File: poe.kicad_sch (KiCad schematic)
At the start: 59 parts, among them IC1 TPS2378DDA, J1 B2B-XH-A_LF__SN_, J6 SS-74800-144, U3 TPS2373-3RGW, U4 URB4805YMD-30WR3

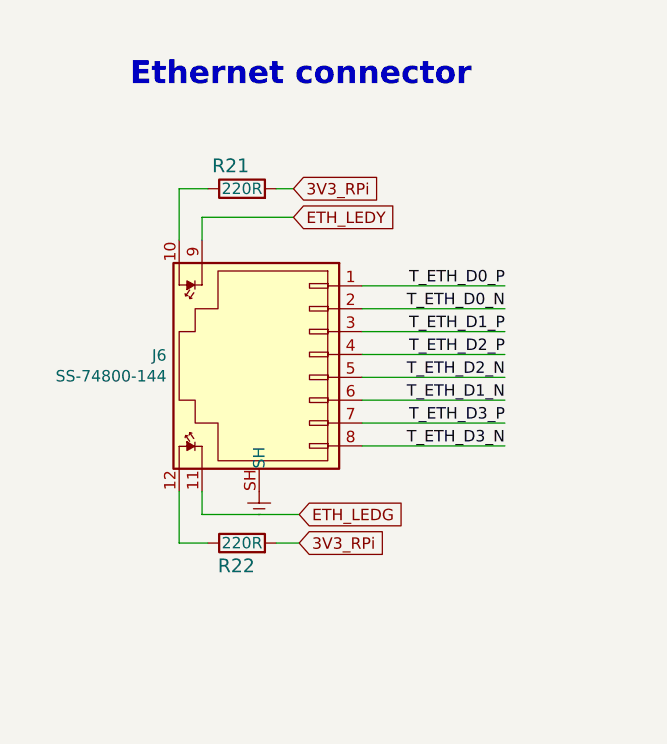
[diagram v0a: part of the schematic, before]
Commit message: Update SS-74800-144 symbol and footprint
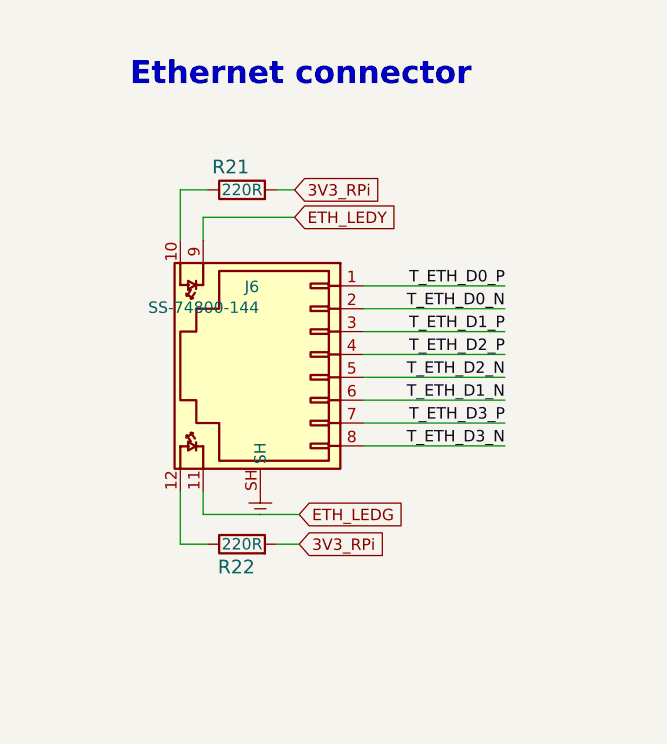
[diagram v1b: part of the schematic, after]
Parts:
- J6: footprint scalenode-cm4-baseboard-footprints:SS-74800-144 -> antmicro-footprints:SS-74800-144; symbol scalenode-cm4-baseboard:SS-74800-144 -> antmicroModularConnectorsJacks:SS-74800-144; Author (none) -> Antmicro; License (none) -> Apache-2.0

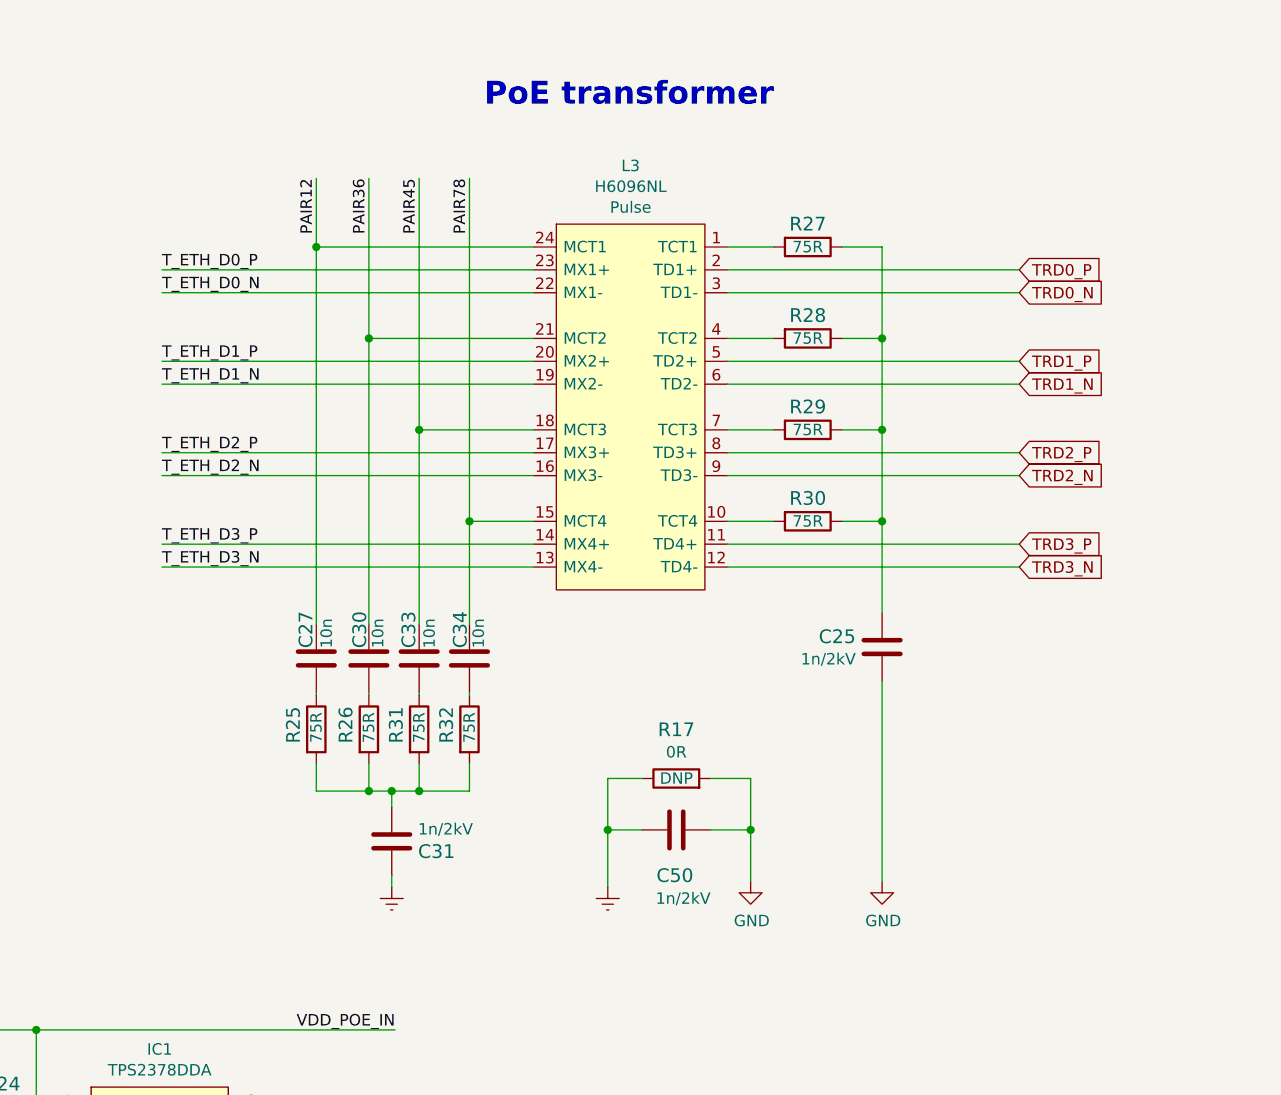
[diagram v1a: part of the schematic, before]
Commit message: Update H6096NL symbol and footprint
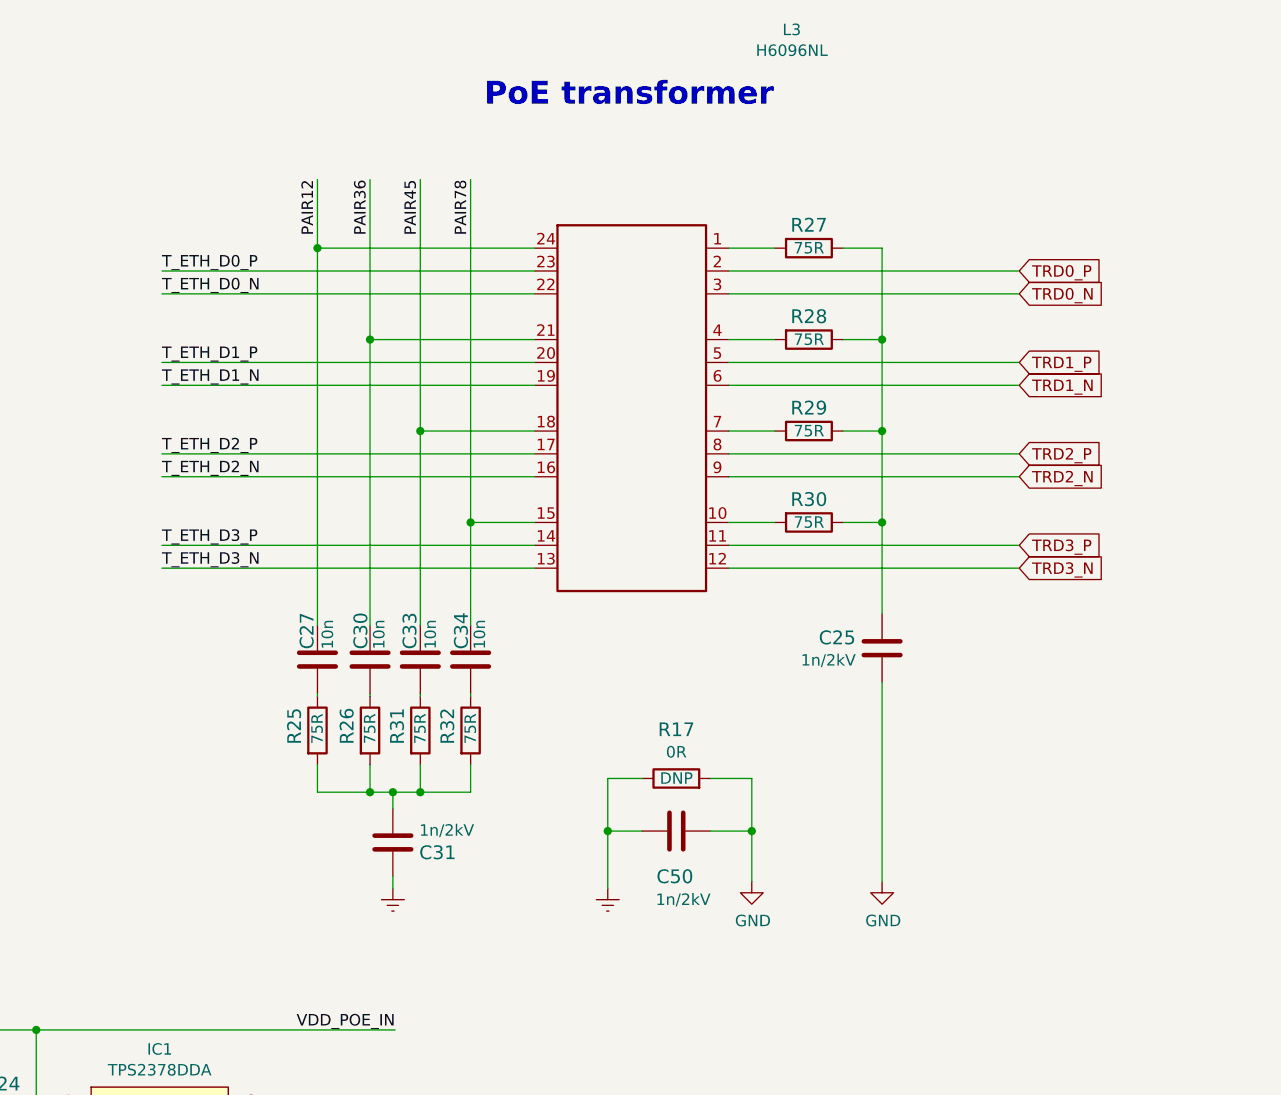
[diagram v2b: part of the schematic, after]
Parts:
- L3: footprint scalenode-cm4-baseboard-footprints:SOIC127P1594X685-24N -> antmicro-footprints:SOIC127P1594X685-24N; symbol scalenode-cm4-baseboard:H6096NL -> antmicroInterfaceDriversReceiversTransceivers:H6096NL; Author (none) -> Antmicro; License (none) -> Apache-2.0

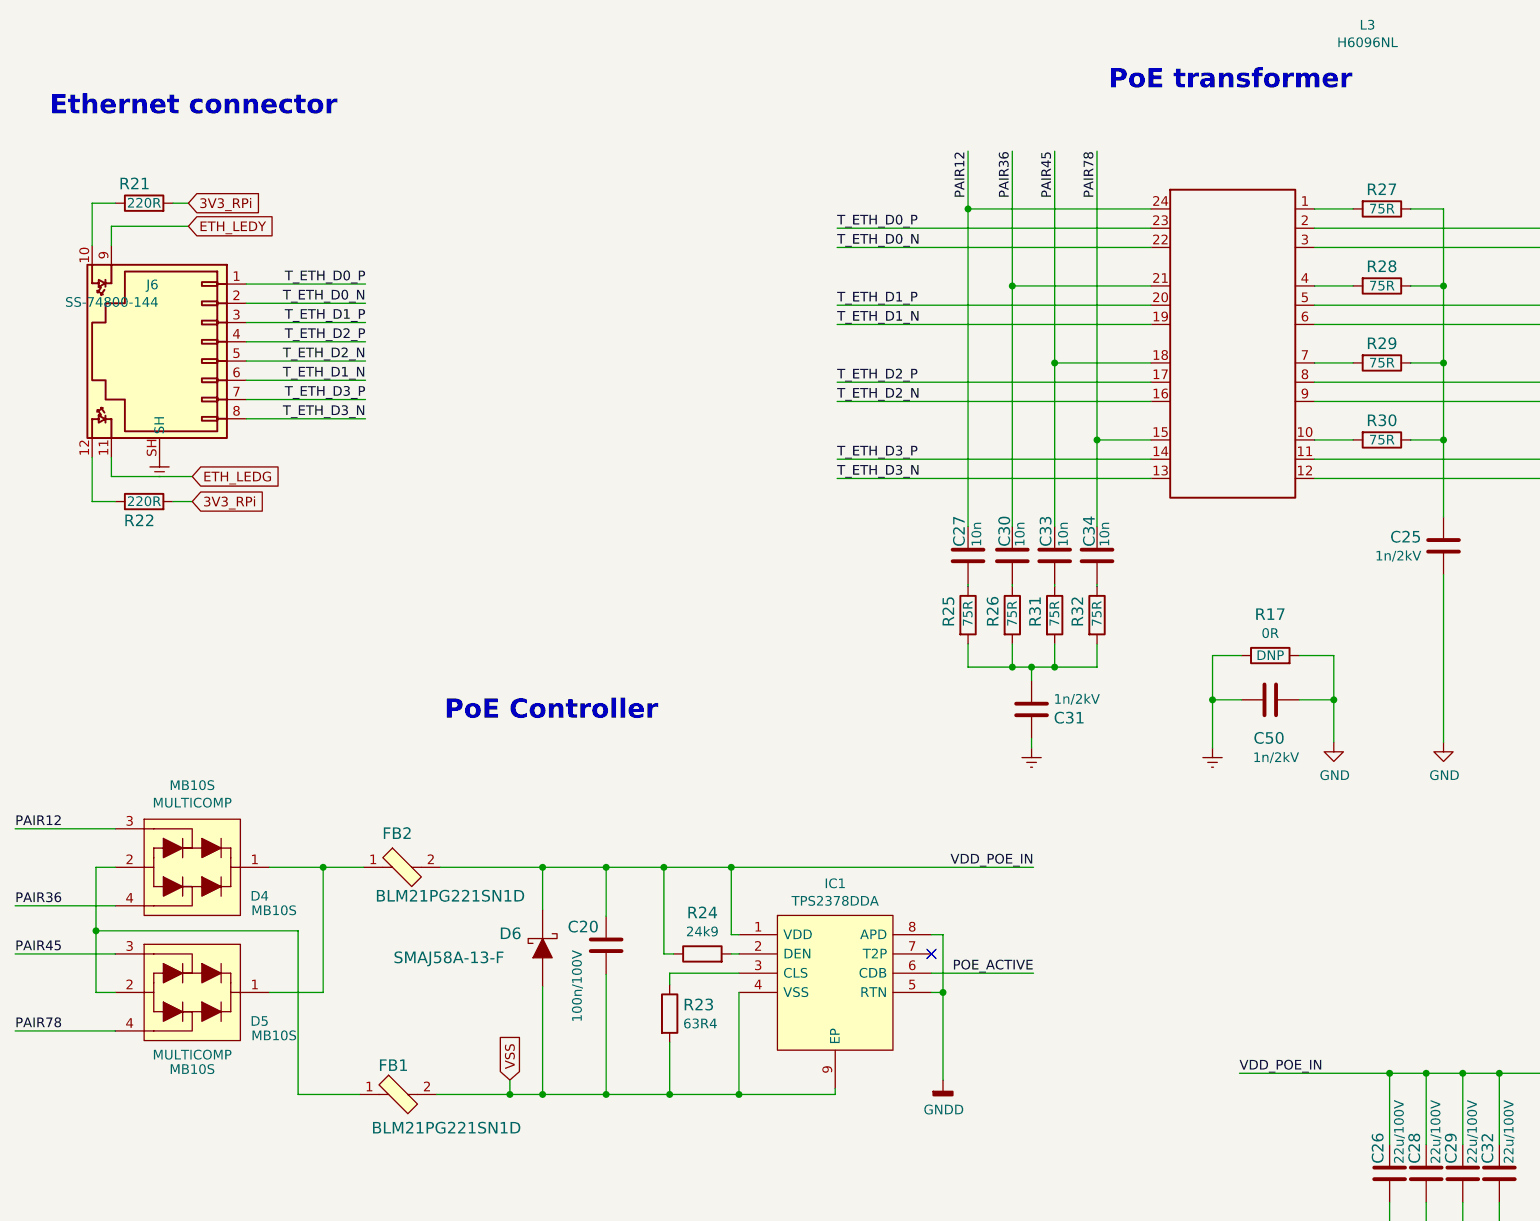
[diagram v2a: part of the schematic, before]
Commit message: Update MB10S symbol and footprint
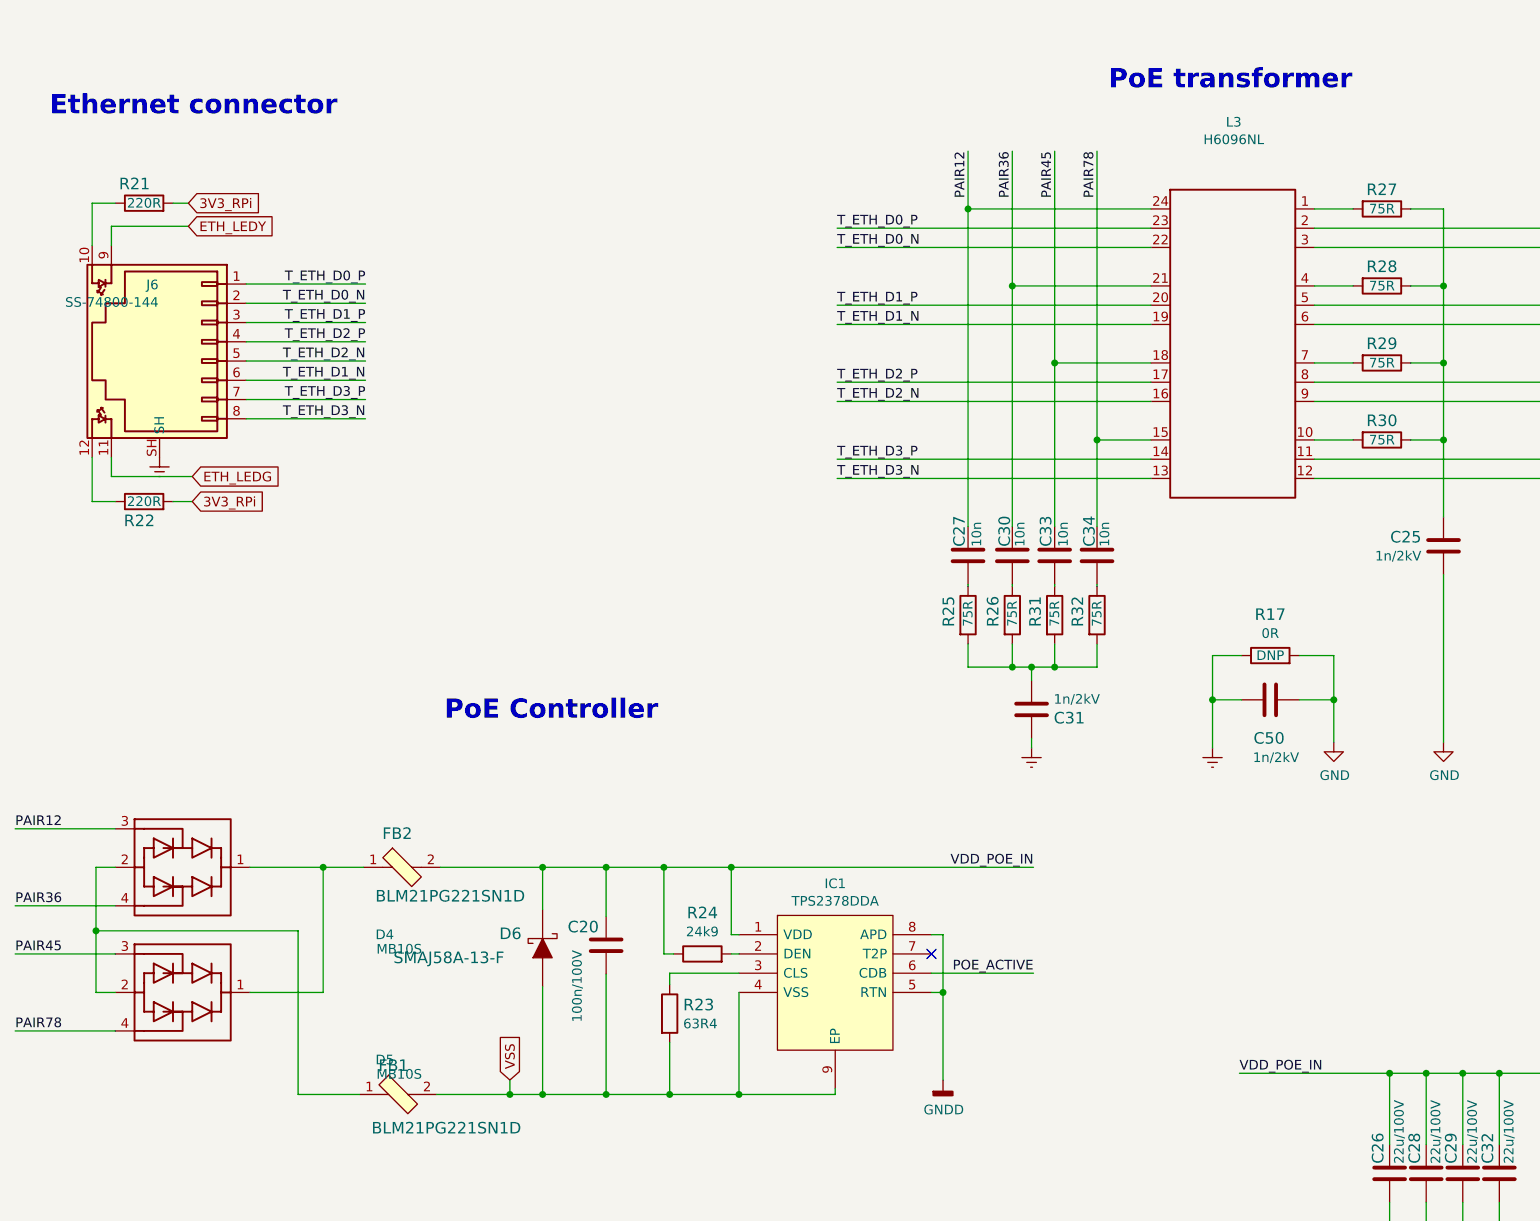
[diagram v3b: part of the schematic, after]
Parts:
- D4, D5: footprint scalenode-cm4-baseboard-footprints:MB10S -> antmicro-footprints:SOIC-4_4.2x5.0mm_P5.7mm; symbol scalenode-cm4-baseboard:MB10S -> antmicroTVSDiodes:MB10S; Author (none) -> Antmicro; License (none) -> Apache-2.0; Manufacturer MULTICOMP -> Multicomp
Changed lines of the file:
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@@
     (stroke (width 0) (type default) (color 0 0 0 0))
   )
-  (wire (pts (xy 73.914 166.37) (xy 81.026 166.37))
+  (wire (pts (xy 71.374 166.37) (xy 81.026 166.37))
     (stroke (width 0) (type default) (color 0 0 0 0))
   )
@@
     (stroke (width 0) (type default) (color 0 0 0 0))
   )
-  (wire (pts (xy 73.914 149.86) (xy 81.026 149.86))
+  (wire (pts (xy 71.374 149.86) (xy 81.026 149.86))
     (stroke (width 0) (type default) (color 0 0 0 0))
   )
@@
   (symbol (lib_id "antmicroInterfaceDriversReceiversTransceivers:H6096NL") (at 211.836 62.992 0) (unit 1)
     (in_bom yes) (on_board yes)
-    (property "Reference" "L3" (id 0) (at 218.821 38.735 0))
-    (property "Value" "H6096NL" (id 1) (at 218.821 41.0464 0))
+    (property "Reference" "L3" (id 0) (at 201.168 51.5366 0))
+    (property "Value" "H6096NL" (id 1) (at 201.168 53.848 0))
     (property "Footprint" "antmicro-footprints:SOIC127P1594X685-24N" (id 2) (at 227.076 70.612 0)
       (effects (font (size 1.27 1.27) (thickness 0.15)) (justify left bottom) hide)
@@
     (pin "2")
   )
-  (symbol (lib_id "scalenode-cm4-baseboard:MB10S") (at 54.864 144.78 0) (unit 1)
+  (symbol (lib_id "antmicroTVSDiodes:MB10S") (at 71.374 149.86 0) (unit 1)
     (in_bom yes) (on_board yes)
-    (property "Reference" "D4" (id 0) (at 72.644 153.67 0))
-    (property "Value" "MB10S" (id 1) (at 74.549 155.575 0))
-    (property "Footprint" "scalenode-cm4-baseboard-footprints:MB10S" (id 2) (at 40.894 146.05 0)
-      (effects (font (size 1.27 1.27)) hide)
+    (property "Reference" "D4" (id 0) (at 89.154 158.75 0))
+    (property "Value" "MB10S" (id 1) (at 91.059 160.655 0))
+    (property "Footprint" "antmicro-footprints:SOIC-4_4.2x5.0mm_P5.7mm" (id 2) (at 86.614 154.94 0)
+      (effects (font (size 1.27 1.27) (thickness 0.15)) (justify left bottom) hide)
     )
-    (property "Datasheet" "http://www.farnell.com/datasheets/2895435.pdf" (id 3) (at 40.894 146.05 0)
-      (effects (font (size 1.27 1.27)) hide)
+    (property "Datasheet" "http://www.farnell.com/datasheets/2895435.pdf" (id 3) (at 86.614 157.48 0)
+      (effects (font (size 1.27 1.27) (thickness 0.15)) (justify left bottom) hide)
+    )
+    (property "MPN" "MB10S" (id 4) (at 86.614 160.02 0)
+      (effects (font (size 1.27 1.27) (thickness 0.15)) (justify left bottom) hide)
+    )
+    (property "Manufacturer" "Multicomp" (id 5) (at 86.614 162.56 0)
+      (effects (font (size 1.27 1.27) (thickness 0.15)) (justify left bottom) hide)
+    )
+    (property "Author" "Antmicro" (id 6) (at 86.614 165.1 0)
+      (effects (font (size 1.27 1.27) (thickness 0.15)) (justify left bottom) hide)
+    )
+    (property "License" "Apache-2.0" (id 7) (at 86.614 167.64 0)
+      (effects (font (size 1.27 1.27) (thickness 0.15)) (justify left bottom) hide)
     )
-    (property "MPN" "MB10S" (id 4) (at 63.754 139.065 0))
-    (property "Manufacturer" "MULTICOMP" (id 5) (at 63.754 141.3764 0))
     (pin "1")
     (pin "2")
@@
     (pin "2")
   )
-  (symbol (lib_id "scalenode-cm4-baseboard:MB10S") (at 54.864 161.29 0) (unit 1)
+  (symbol (lib_id "antmicroTVSDiodes:MB10S") (at 71.374 166.37 0) (unit 1)
     (in_bom yes) (on_board yes)
-    (property "Reference" "D5" (id 0) (at 72.644 170.18 0))
-    (property "Value" "MB10S" (id 1) (at 74.549 172.085 0))
-    (property "Footprint" "scalenode-cm4-baseboard-footprints:MB10S" (id 2) (at 40.894 162.56 0)
-      (effects (font (size 1.27 1.27)) hide)
+    (property "Reference" "D5" (id 0) (at 89.154 175.26 0))
+    (property "Value" "MB10S" (id 1) (at 91.059 177.165 0))
+    (property "Footprint" "antmicro-footprints:SOIC-4_4.2x5.0mm_P5.7mm" (id 2) (at 86.614 171.45 0)
+      (effects (font (size 1.27 1.27) (thickness 0.15)) (justify left bottom) hide)
     )
-    (property "Datasheet" "http://www.farnell.com/datasheets/2895435.pdf" (id 3) (at 40.894 162.56 0)
-      (effects (font (size 1.27 1.27)) hide)
+    (property "Datasheet" "http://www.farnell.com/datasheets/2895435.pdf" (id 3) (at 86.614 173.99 0)
+      (effects (font (size 1.27 1.27) (thickness 0.15)) (justify left bottom) hide)
+    )
+    (property "MPN" "MB10S" (id 4) (at 86.614 176.53 0)
+      (effects (font (size 1.27 1.27) (thickness 0.15)) (justify left bottom) hide)
+    )
+    (property "Manufacturer" "Multicomp" (id 5) (at 86.614 179.07 0)
+      (effects (font (size 1.27 1.27) (thickness 0.15)) (justify left bottom) hide)
+    )
+    (property "Author" "Antmicro" (id 6) (at 86.614 181.61 0)
+      (effects (font (size 1.27 1.27) (thickness 0.15)) (justify left bottom) hide)
+    )
+    (property "License" "Apache-2.0" (id 7) (at 86.614 184.15 0)
+      (effects (font (size 1.27 1.27) (thickness 0.15)) (justify left bottom) hide)
     )
-    (property "MPN" "MB10S" (id 4) (at 63.754 176.53 0))
-    (property "Manufacturer" "MULTICOMP" (id 5) (at 63.754 174.625 0))
     (pin "1")
     (pin "2")
